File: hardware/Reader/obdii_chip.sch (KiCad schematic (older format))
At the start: 19 parts

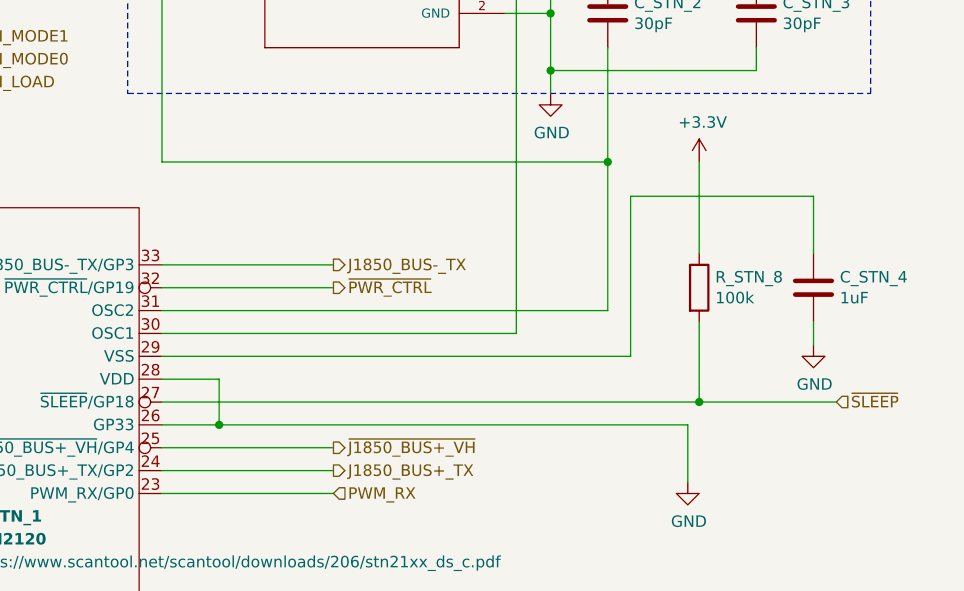
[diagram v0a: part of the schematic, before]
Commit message: Fixed numerous bugs in design for Reader Schematic and PCB
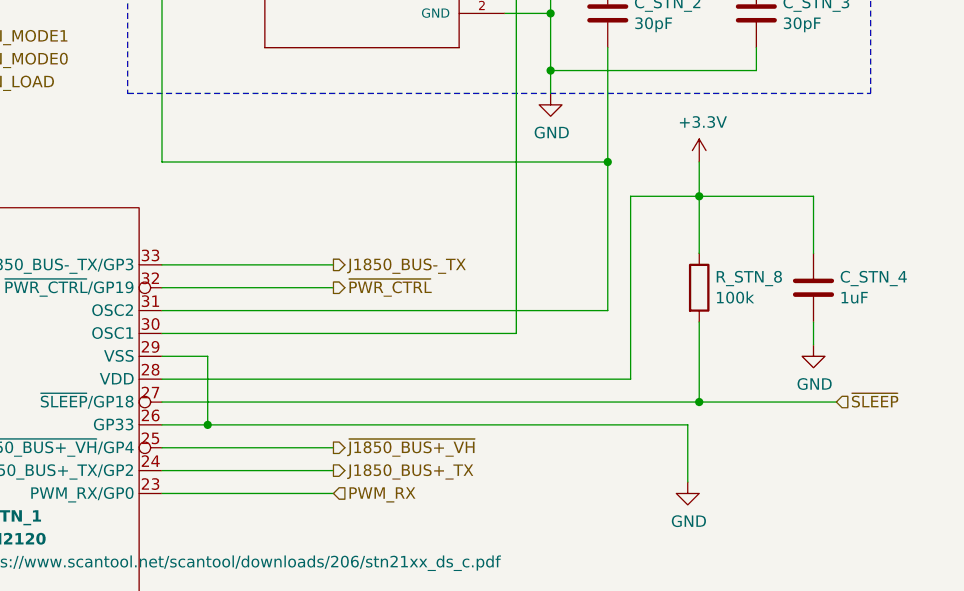
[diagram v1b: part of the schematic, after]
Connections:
- net +3V3: now also C_STN_4.1, U_STN_1.28 (VDD)
- net GND: now also U_STN_1.29 (VSS); no longer U_STN_1.28 (VDD)
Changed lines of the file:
@@
 	1    0    0    -1
 $EndComp
-Wire Wire Line
-	7100 3100 7350 3100
-Wire Wire Line
-	7350 3100 7350 3300
-Wire Wire Line
-	7100 3300 7350 3300
-Connection ~ 7350 3300
 Text HLabel 7850 2600 2    50   Output ~ 0
 J1850_BUS-_TX
@@
 Wire Wire Line
 	9400 3300 9400 3550
-Wire Wire Line
-	7350 3300 9400 3300
 $Comp
 L ECS-2033-160-AU:ECS-2033-160-AU Y_STN_1
@@
 	7100 1350 7100 2150
 Wire Wire Line
-	9450 2550 9450 2150
-Wire Wire Line
 	9450 2850 9450 3200
 Wire Wire Line
@@
 	9450 3200 10050 3200
 Wire Wire Line
-	7100 3000 9150 3000
-Wire Wire Line
-	9150 3000 9150 2300
-Wire Wire Line
-	9150 2300 9950 2300
+	9150 2300 9450 2300
 Wire Wire Line
 	3950 4000 4750 4000
@@
 Wire Wire Line
 	5900 7200 5900 7050
+Wire Wire Line
+	7100 3300 7300 3300
+Wire Wire Line
+	7100 3000 7300 3000
+Wire Wire Line
+	7300 3000 7300 3300
+Connection ~ 7300 3300
+Wire Wire Line
+	7300 3300 9400 3300
+Wire Wire Line
+	7100 3100 9150 3100
+Wire Wire Line
+	9150 2300 9150 3100
+Wire Wire Line
+	9450 2150 9450 2300
+Connection ~ 9450 2300
+Wire Wire Line
+	9450 2300 9950 2300
+Wire Wire Line
+	9450 2550 9450 2300
 $EndSCHEMATC

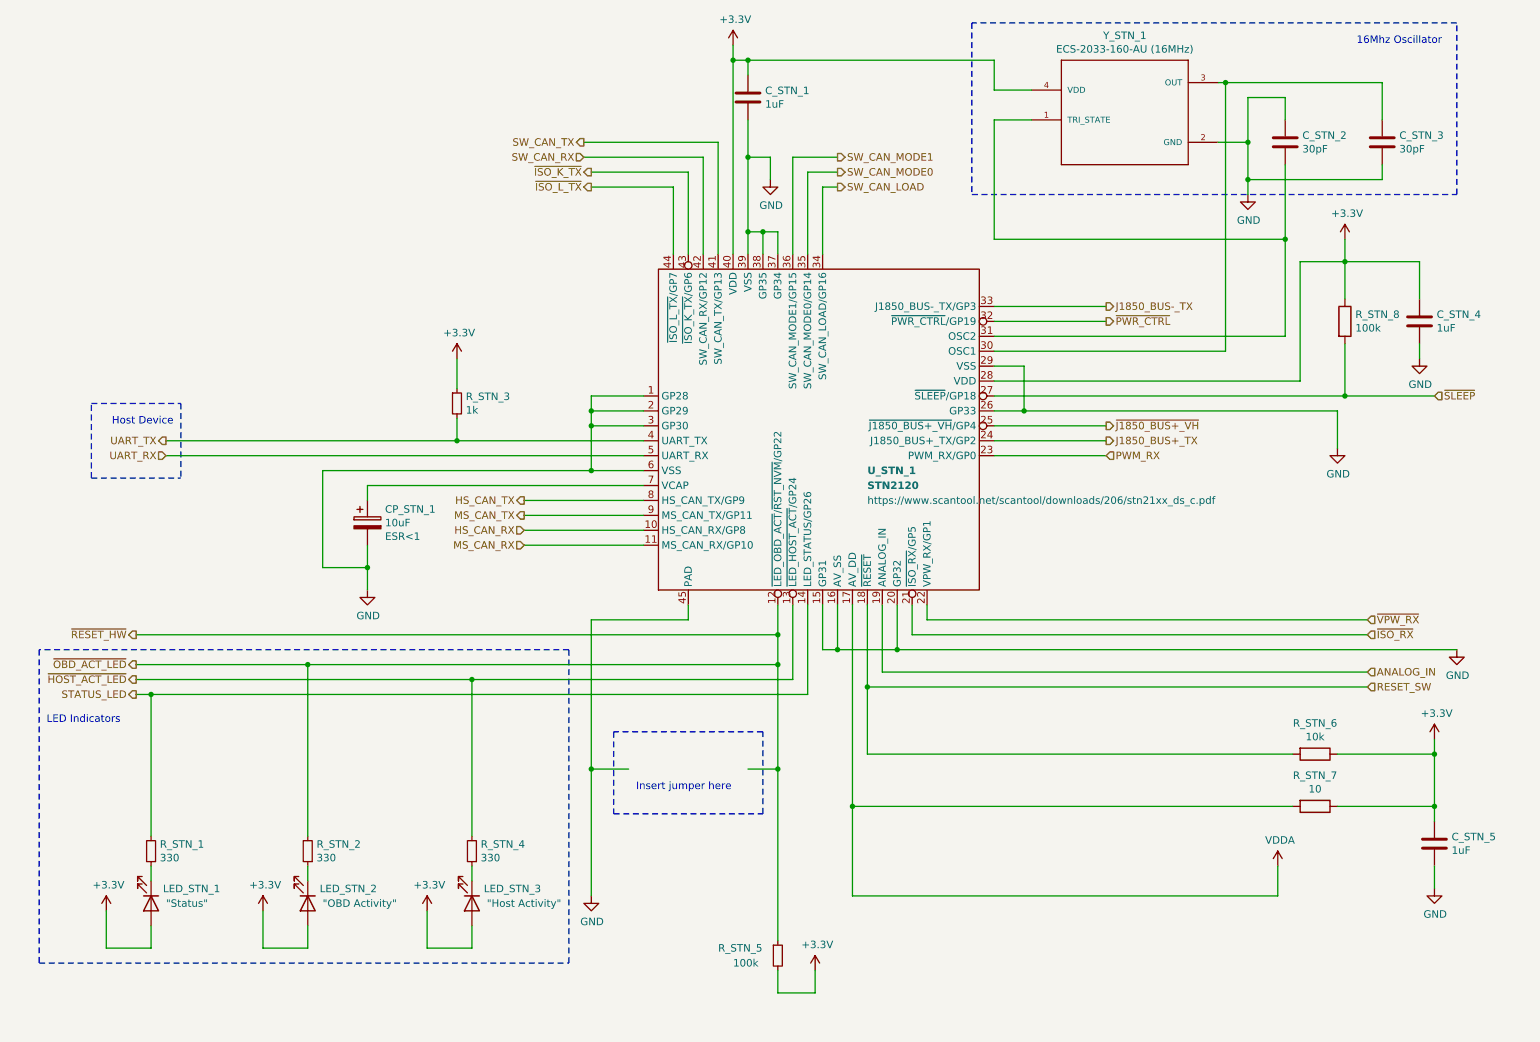
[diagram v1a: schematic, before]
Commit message: Updated reader schematic to v0.0.5 by adding ESP32, removing unused transceivers, fixed design flaws, increased header pins and fixed footprints. Working on reader PCB design
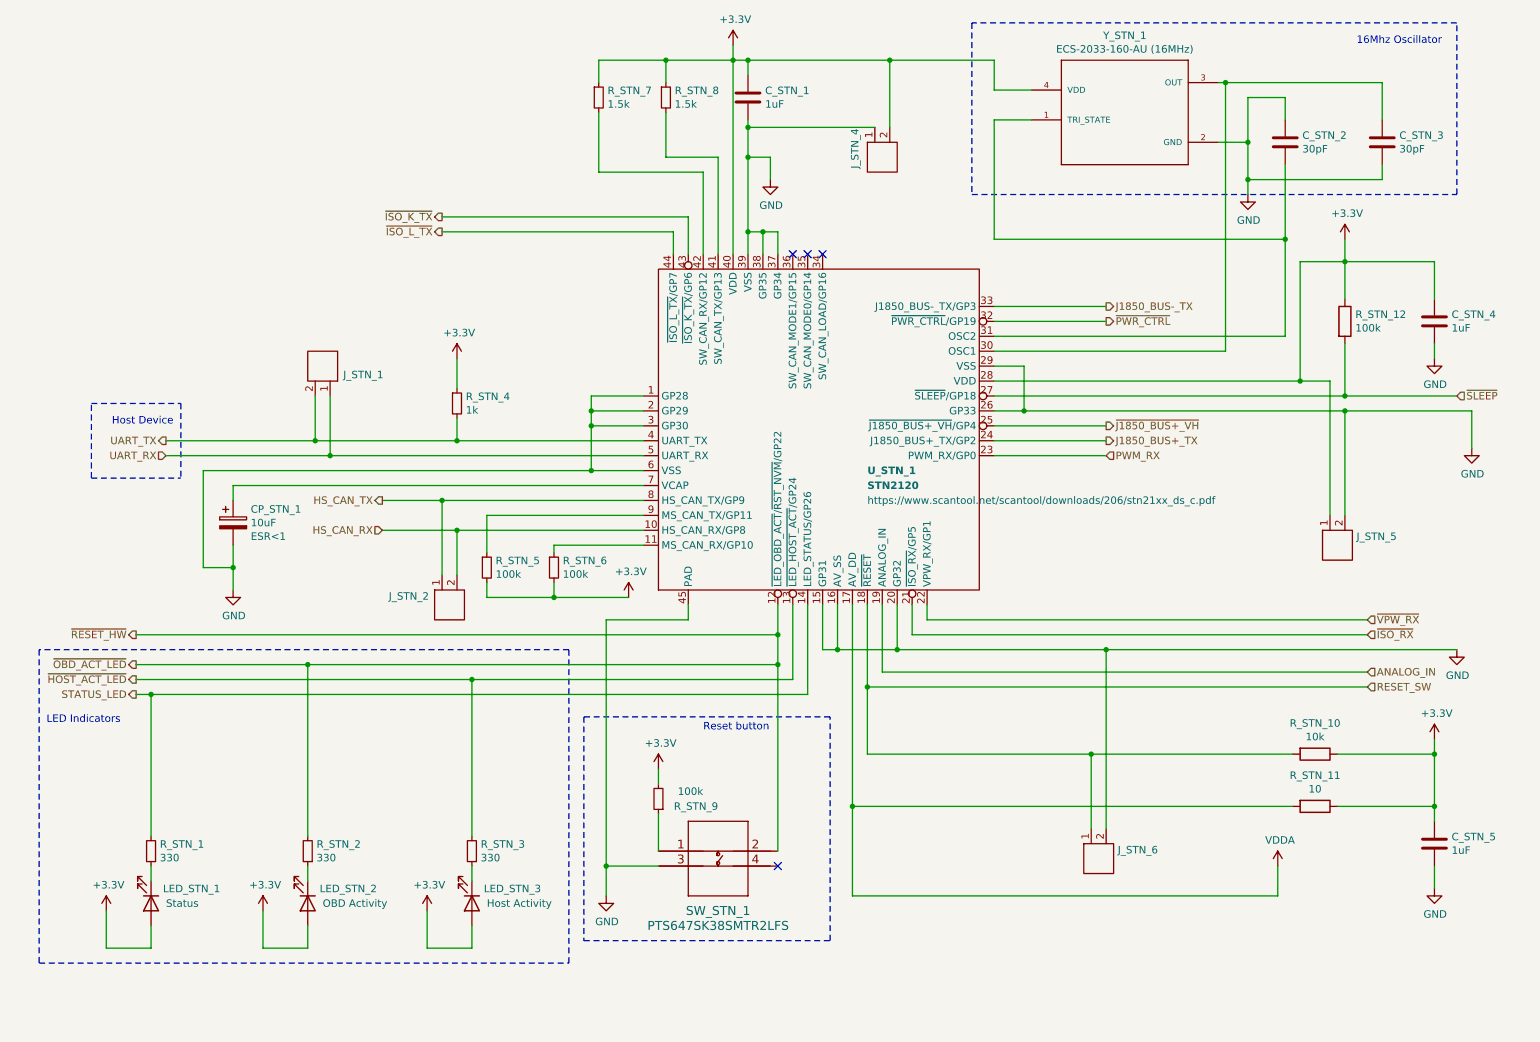
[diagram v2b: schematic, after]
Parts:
- added J_STN_1, J_STN_2, J_STN_4, J_STN_5, J_STN_6: Header_Pin_2, Connector_PinHeader_2.54mm:PinHeader_1x02_P2.54mm_Vertical, symbol CANtech:Header_Pin_2
- added R_STN_5, R_STN_6: 100k, footprints:RESC1608X55N, symbol Device:R_Small
- added R_STN_7, R_STN_8: 1.5k, footprints:RESC1607X60N, symbol Device:R_Small
- added SW_STN_1: PTS647SK38SMTR2LFS, footprints:PTS647SK38SMTR2LFS, symbol PTS647SK38SMTR2LFS:PTS647SK38SMTR2LFS
- LED_STN_1: value \"Status\" -> Status
- LED_STN_2: value \"OBD Activity\" -> OBD Activity
- LED_STN_3: value \"Host Activity\" -> Host Activity
- R_STN_11: renamed from R_STN_7; footprint footprints:RESC1005X40N -> footprints:RESC1608X55N; Manufacturer Bourns Inc. -> Yageo; Part Name CR0402-FX-10R0GLF -> RE0603FRE0710RL; digikeypn CR0402-FX-10R0GLFCT-ND -> 13-RE0603FRE0710RLCT-ND
- U_STN_1: footprint Package_DFN_QFN:QFN-44-1EP_8x8mm_P0.65mm_EP6.45x6.45mm_ThermalVias -> footprints:CANtech-STN2120-QFN-44-1EP_8x8mm; Vendor ScanTool -> OBD Solutions
- renumbered R_STN_6 to R_STN_10, R_STN_8 to R_STN_12, R_STN_4 to R_STN_3, R_STN_3 to R_STN_4, R_STN_5 to R_STN_9
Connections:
- net +3V3: now also J_STN_4.2, J_STN_5.1, R_STN_5.2, R_STN_6.2, R_STN_7.1, R_STN_8.1
- net GND: now also J_STN_4.1, J_STN_5.2, J_STN_6.2, SW_STN_1.3
- net HS_CAN_RX: now also J_STN_2.2
- net HS_CAN_TX: now also J_STN_2.1
- net RESET_SW: now also J_STN_6.1
- net UART_RX: now also J_STN_1.1
- net UART_TX: now also J_STN_1.2
- net ~OBD_ACT_LED~: now also SW_STN_1.2; no longer R_STN_9.1
- net MS_CAN_RX: no longer names the net of U_STN_1.11 (MS_CAN_RX/GP10)
- net MS_CAN_RX: now also R_STN_6.1
- net MS_CAN_TX: no longer names the net of U_STN_1.9 (MS_CAN_TX/GP11)
- net MS_CAN_TX: now also R_STN_5.1
- net SW_CAN_LOAD: no longer names the net of U_STN_1.34 (SW_CAN_LOAD/GP16)
- net SW_CAN_MODE0: no longer names the net of U_STN_1.35 (SW_CAN_MODE0/GP14)
- net SW_CAN_MODE1: no longer names the net of U_STN_1.36 (SW_CAN_MODE1/GP15)
- net SW_CAN_RX: no longer names the net of U_STN_1.42 (SW_CAN_RX/GP12)
- net SW_CAN_RX: now also R_STN_7.2
- net SW_CAN_TX: no longer names the net of U_STN_1.41 (SW_CAN_TX/GP13)
- net SW_CAN_TX: now also R_STN_8.2
- new net: R_STN_9.1, SW_STN_1.1
- no-connect marks 0 -> 4
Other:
- note added: "Reset button"
- note removed: "Insert jumper here"
- moved on the sheet: CP_STN_1, C_STN_4, R_STN_9
